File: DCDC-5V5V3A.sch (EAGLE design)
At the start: 31 parts, among them U1 TPS63020DSJR

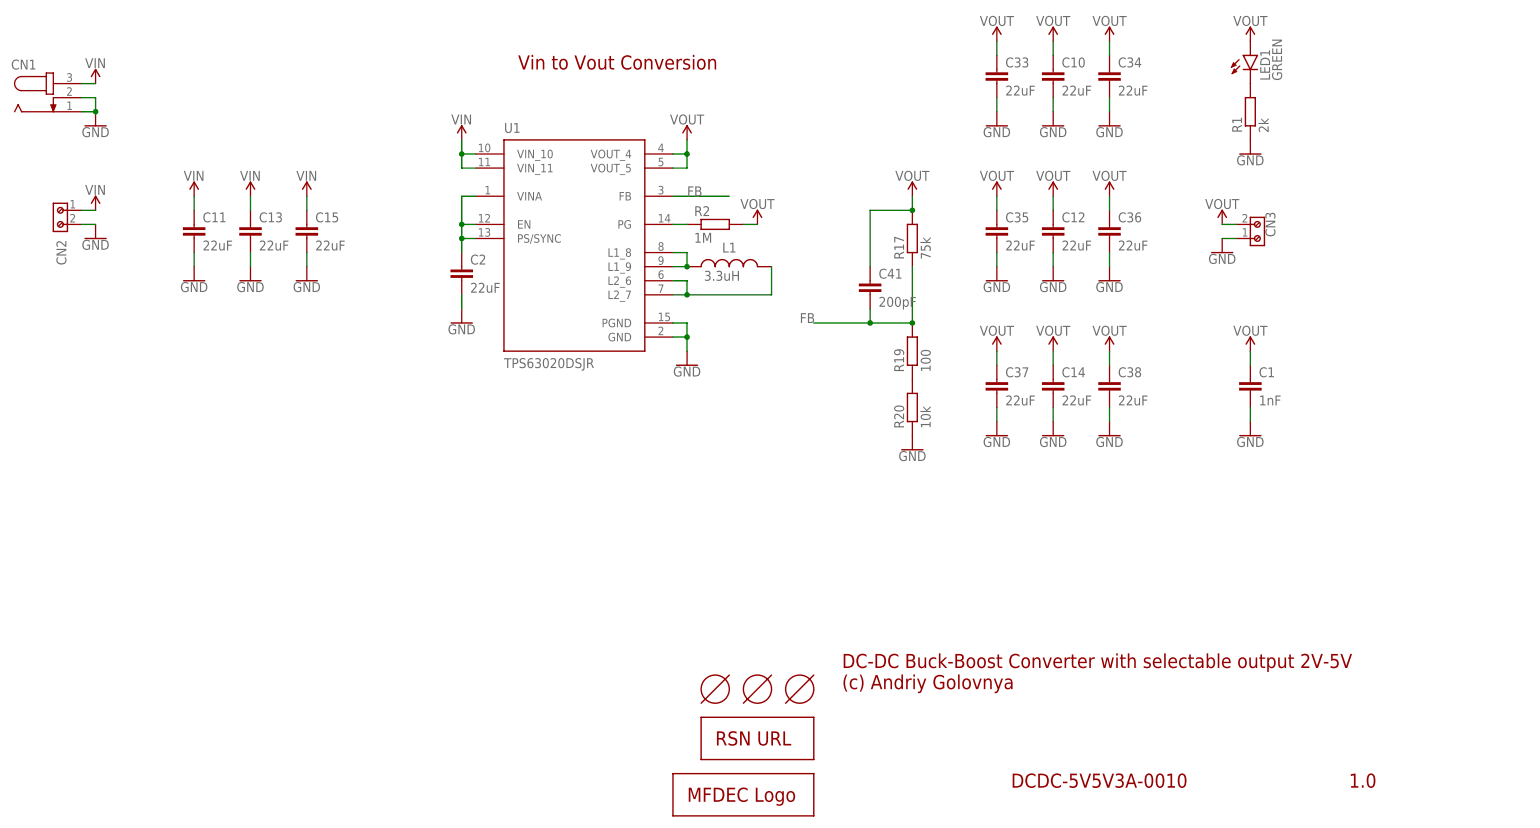
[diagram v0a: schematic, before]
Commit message: Improved schematics and routing of 5V-5V board. Generated PDF schematics. Generated PNG preview. Generated CAM files.
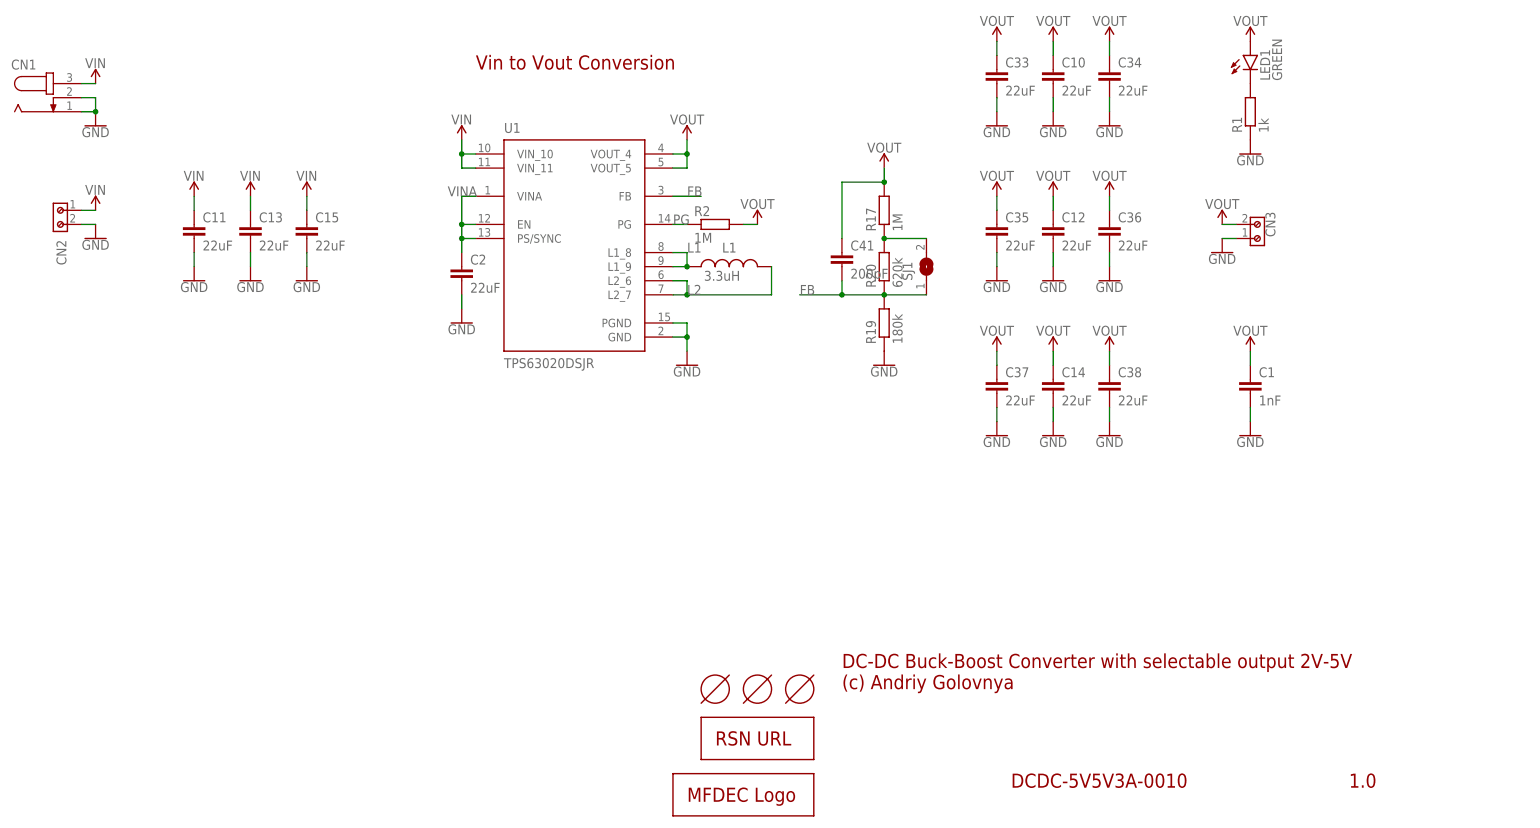
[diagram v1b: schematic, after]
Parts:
- added SJ1: (no value), _my_jumpers:SJ
- R1: value 2k -> 1k
- R17: value 75k -> 1M
- R19: value 100 -> 180k
- R20: value 10k -> 620k
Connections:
- net N$3 renamed L1
- net N$4 renamed PG
- net N$5 renamed L2
- net N$7 renamed VINA
- net FB: now also R20.1, SJ1.1; no longer R17.1
- net GND: now also R19.1; no longer R20.1
- net N$2: now also R17.1, SJ1.2; no longer R19.1
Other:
- moved on the sheet: C41, R17, R19, R20

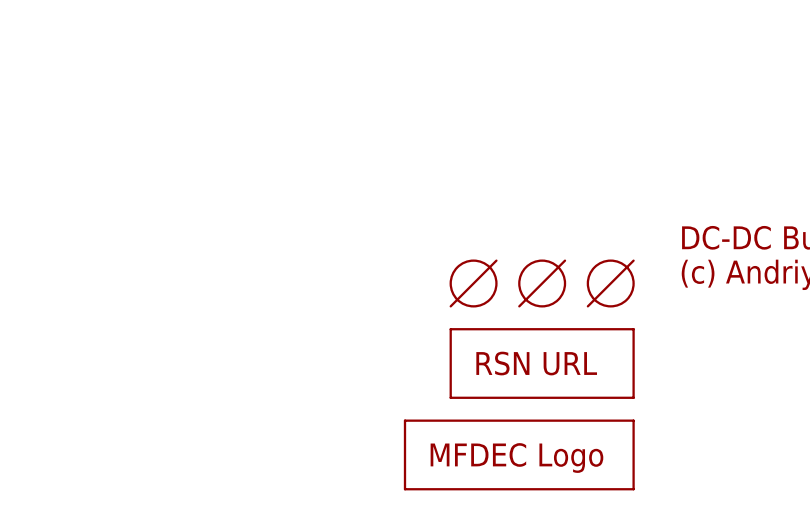
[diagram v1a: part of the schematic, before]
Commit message: Moved some texts and tooling holes a bit. Generated CAM files. Generated PNG preview. Generated PDF schematics. Renamed BoM and PnP files.
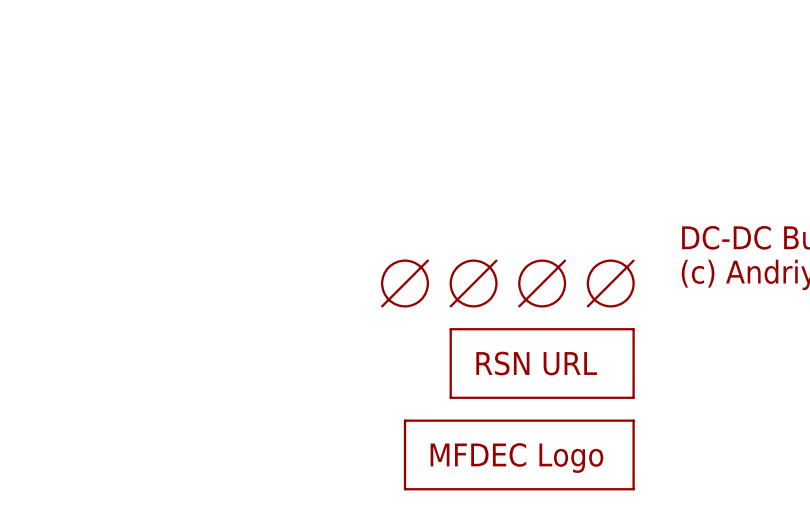
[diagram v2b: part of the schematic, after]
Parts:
- added HOLE4: TOOLINGHOLE, _my_fiducia:TOOLINGHOLE
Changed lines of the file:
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@@
 <part name="SUPPLY11" library="SparkFun-PowerSymbols" library_urn="urn:adsk.eagle:library:530" deviceset="VOUT" device=""/>
 <part name="SJ1" library="_my_jumpers" deviceset="SJ" device=""/>
+<part name="HOLE4" library="_my_fiducia" deviceset="TOOLINGHOLE" device=""/>
 </parts>
 <sheets>
@@
 <attribute name="VALUE" x="184.15" y="99.06" size="1.778" layer="96" rot="R90"/>
 </instance>
+<instance part="HOLE4" gate="G$1" x="134.62" y="25.4" smashed="yes"/>
 </instances>
 <busses>

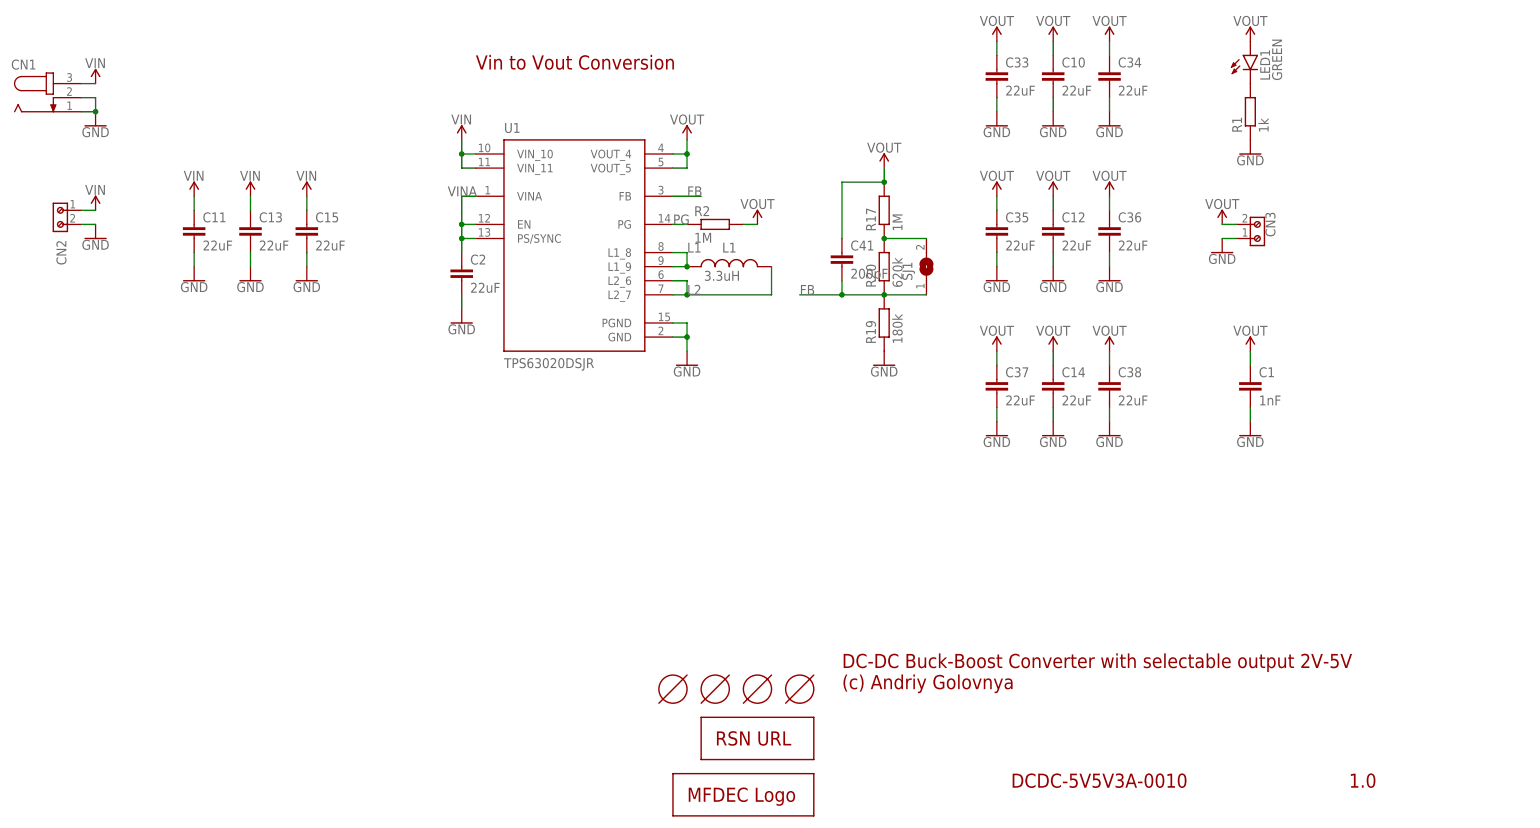
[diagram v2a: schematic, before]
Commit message: Added 200k resistor to improve voltage output. Generated CAM files. Generated PNG preview. Generated PDF schematics. Adjusted BoM and PnP files. Adjusted Excel calculator.
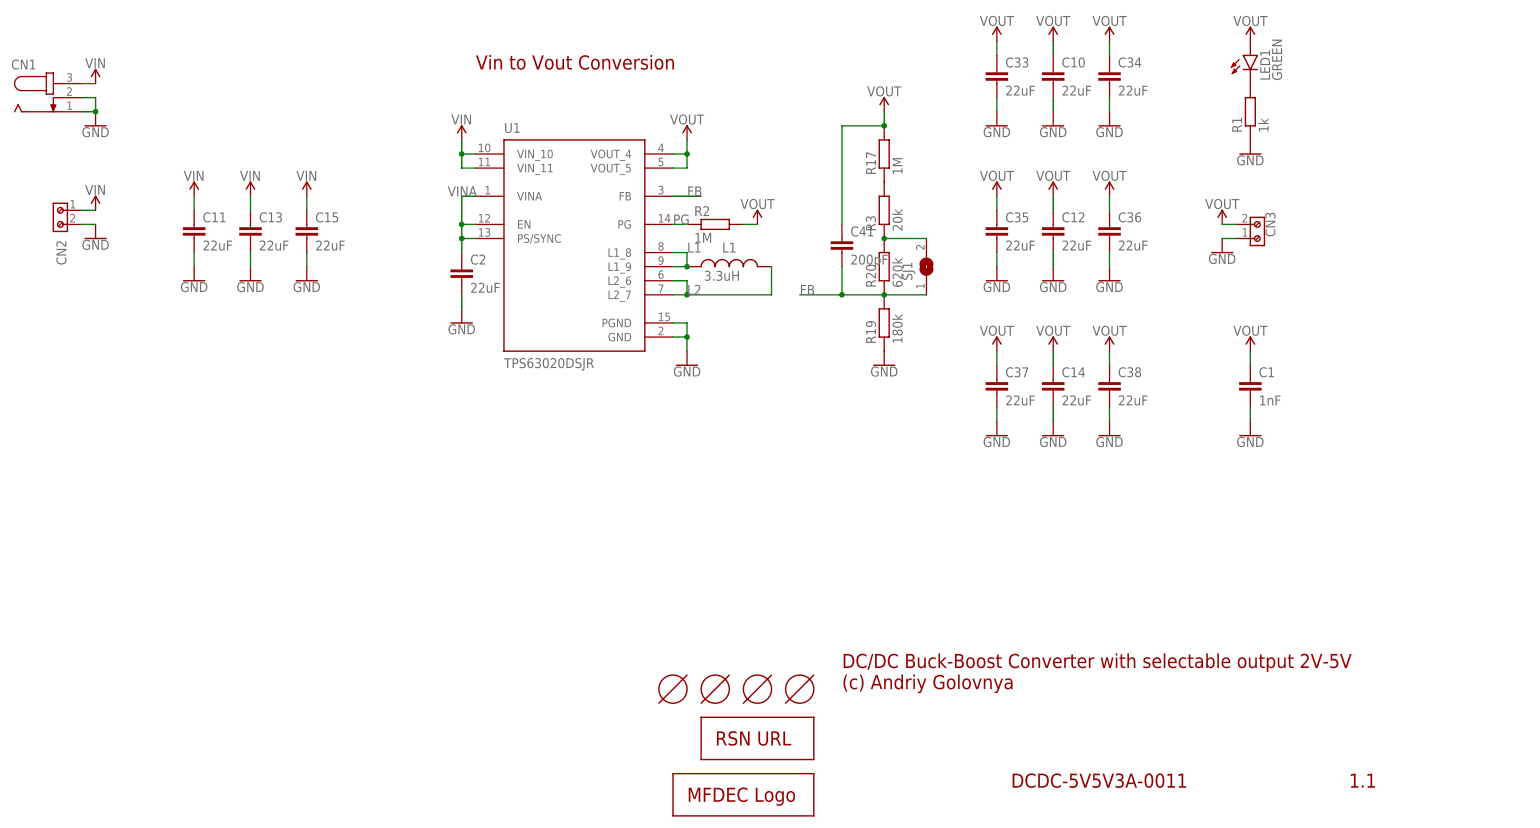
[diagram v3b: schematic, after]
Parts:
- added R3: 20k, rcl:R-EU_R0603
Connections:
- new net N$3: R20.2, R3.1, SJ1.2
- net N$2: now also R3.2; no longer R20.2, SJ1.2
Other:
- note added: "1.1"
- note added: "DC/DC Buck-Boost Converter with selectable output 2V-5V (c) Andriy Golovnya"
- note added: "DCDC-5V5V3A-0011"
- note removed: "1.0"
- note removed: "DC-DC Buck-Boost Converter with selectable output 2V-5V (c) Andriy Golovnya"
- note removed: "DCDC-5V5V3A-0010"
- moved on the sheet: C41, R17
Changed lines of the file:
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@@
 <part name="SJ1" library="_my_jumpers" deviceset="SJ" device=""/>
 <part name="HOLE4" library="_my_fiducia" deviceset="TOOLINGHOLE" device=""/>
+<part name="R3" library="rcl" library_urn="urn:adsk.eagle:library:334" deviceset="R-EU_" device="R0603" package3d_urn="urn:adsk.eagle:package:23555/3" value="20k"/>
 </parts>
 <sheets>
 <sheet>
 <plain>
-<text x="256.54" y="7.62" size="2.54" layer="94">1.0</text>
-<text x="195.58" y="7.62" size="2.54" layer="94">DCDC-5V5V3A-0010</text>
-<text x="165.1" y="25.4" size="2.54" layer="94">DC-DC Buck-Boost Converter with selectable output 2V-5V
+<text x="256.54" y="7.62" size="2.54" layer="94">1.1</text>
+<text x="195.58" y="7.62" size="2.54" layer="94">DCDC-5V5V3A-0011</text>
+<text x="165.1" y="25.4" size="2.54" layer="94">DC/DC Buck-Boost Converter with selectable output 2V-5V
 (c) Andriy Golovnya</text>
 <text x="99.06" y="137.16" size="2.54" layer="94">Vin to Vout Conversion</text>
@@
 <attribute name="VALUE" x="140.208" y="99.06" size="1.778" layer="96"/>
 </instance>
-<instance part="SUPPLY45" gate="G$1" x="172.72" y="119.38" smashed="yes">
-<attribute name="VALUE" x="172.72" y="122.174" size="1.778" layer="96" align="bottom-center"/>
+<instance part="SUPPLY45" gate="G$1" x="172.72" y="129.54" smashed="yes">
+<attribute name="VALUE" x="172.72" y="132.334" size="1.778" layer="96" align="bottom-center"/>
 </instance>
 <instance part="GND52" gate="1" x="137.16" y="83.82" smashed="yes">
@@
 <attribute name="VALUE" x="96.52" y="127.254" size="1.778" layer="96" align="bottom-center"/>
 </instance>
-<instance part="R17" gate="G$1" x="172.72" y="111.76" smashed="yes" rot="R90">
-<attribute name="NAME" x="171.2214" y="107.95" size="1.778" layer="95" rot="R90"/>
-<attribute name="VALUE" x="176.022" y="107.95" size="1.778" layer="96" rot="R90"/>
+<instance part="R17" gate="G$1" x="172.72" y="121.92" smashed="yes" rot="R90">
+<attribute name="NAME" x="171.2214" y="118.11" size="1.778" layer="95" rot="R90"/>
+<attribute name="VALUE" x="176.022" y="118.11" size="1.778" layer="96" rot="R90"/>
 </instance>
 <instance part="R19" gate="G$1" x="172.72" y="91.44" smashed="yes" rot="R90">
@@
 <attribute name="VALUE" x="172.72" y="83.566" size="1.778" layer="96" align="top-center"/>
 </instance>
-<instance part="C41" gate="G$1" x="165.1" y="104.14" smashed="yes">
-<attribute name="NAME" x="166.624" y="104.521" size="1.778" layer="95"/>
-<attribute name="VALUE" x="166.624" y="99.441" size="1.778" layer="96"/>
+<instance part="C41" gate="G$1" x="165.1" y="106.68" smashed="yes">
+<attribute name="NAME" x="166.624" y="107.061" size="1.778" layer="95"/>
+<attribute name="VALUE" x="166.624" y="101.981" size="1.778" layer="96"/>
 </instance>
 <instance part="SUPPLY2" gate="G$1" x="68.58" y="114.3" smashed="yes">
@@
 </instance>
 <instance part="HOLE4" gate="G$1" x="134.62" y="25.4" smashed="yes"/>
+<instance part="R3" gate="G$1" x="172.72" y="111.76" smashed="yes" rot="R90">
+<attribute name="NAME" x="171.2214" y="107.95" size="1.778" layer="95" rot="R90"/>
+<attribute name="VALUE" x="176.022" y="107.95" size="1.778" layer="96" rot="R90"/>
+</instance>
 </instances>
 <busses>
@@
 <pinref part="SUPPLY45" gate="G$1" pin="VOUT"/>
 <pinref part="R17" gate="G$1" pin="2"/>
-<wire x1="172.72" y1="116.84" x2="172.72" y2="119.38" width="0.1524" layer="91"/>
+<wire x1="172.72" y1="127" x2="172.72" y2="129.54" width="0.1524" layer="91"/>
 <pinref part="C41" gate="G$1" pin="1"/>
-<wire x1="165.1" y1="106.68" x2="165.1" y2="116.84" width="0.1524" layer="91"/>
-<wire x1="165.1" y1="116.84" x2="172.72" y2="116.84" width="0.1524" layer="91"/>
-<junction x="172.72" y="116.84"/>
+<wire x1="165.1" y1="109.22" x2="165.1" y2="127" width="0.1524" layer="91"/>
+<wire x1="165.1" y1="127" x2="172.72" y2="127" width="0.1524" layer="91"/>
+<junction x="172.72" y="127"/>
 </segment>
 <segment>
@@
 <label x="157.48" y="96.52" size="1.778" layer="95"/>
 <pinref part="C41" gate="G$1" pin="2"/>
-<wire x1="165.1" y1="99.06" x2="165.1" y2="96.52" width="0.1524" layer="91"/>
+<wire x1="165.1" y1="101.6" x2="165.1" y2="96.52" width="0.1524" layer="91"/>
 <wire x1="165.1" y1="96.52" x2="157.48" y2="96.52" width="0.1524" layer="91"/>
 <pinref part="R19" gate="G$1" pin="2"/>
@@
 <segment>
 <pinref part="R17" gate="G$1" pin="1"/>
+<pinref part="R3" gate="G$1" pin="2"/>
+</segment>
+</net>
+<net name="N$3" class="0">
+<segment>
 <pinref part="R20" gate="G$1" pin="2"/>
-<wire x1="172.72" y1="106.68" x2="180.34" y2="106.68" width="0.1524" layer="91"/>
+<pinref part="R3" gate="G$1" pin="1"/>
+<pinref part="SJ1" gate="1" pin="2"/>
+<wire x1="180.34" y1="106.68" x2="172.72" y2="106.68" width="0.1524" layer="91"/>
 <junction x="172.72" y="106.68"/>
-<pinref part="SJ1" gate="1" pin="2"/>
-</segment>
-</net>
+</segment>
+</net>
